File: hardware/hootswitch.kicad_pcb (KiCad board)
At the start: 2 copper layers, 100 x 88 mm, 127 parts, among them J1 Mini-DIN-4-G, J10 POWSEL, J11 TWI, J12 TWI, J2 Mini-DIN-4-G, J3 Mini-DIN-4-G, J4 Mini-DIN-4-G, J5 Mini-DIN-4-G, J6 Mini-DIN-4-G, J7 Barrel_Jack_MountingPin, J8 EXT_POW, J9 SW1, Q1 MMBT3904, Q10 MMBT3904, Q11 MMBT3904, Q12 MMBT3904, Q13 MMBT3904, Q14 MMBT3904, Q15 MMBT3904, Q16 MMBT3904, Q2 MMBT3904, Q3 MMBT3904, Q4 MMBT3904, Q5 MMBT3904, Q6 MMBT3904, Q7 MMBT3904, Q8 MMBT3904, Q9 MMBT3904, SW1 Switch1, U1 PicoW, U10 LTV-357T, U11 LTV-357T, U2 LM1117-5.0, U3 ADuM1201AR, U4 ADuM1201AR, U5 ADuM1201AR, U6 ADuM1201AR, U7 ADuM1201AR, U8 LTV-357T, U9 LTV-357T

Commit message: Increase resistance for the green LEDs
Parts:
- R14, R15, R16, R17: value 1K -> 1K8
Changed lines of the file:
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@@
       (effects (font (size 1 1) (thickness 0.15)))
     )
-    (fp_text value "1K" (at 0 1.43 90) (layer "F.Fab")
+    (fp_text value "1K8" (at 0 1.43 90) (layer "F.Fab")
       (effects (font (size 1 1) (thickness 0.15)))
     )
@@
       (effects (font (size 1 1) (thickness 0.15)))
     )
-    (fp_text value "1K" (at 0 1.43 90) (layer "F.Fab")
+    (fp_text value "1K8" (at 0 1.43 90) (layer "F.Fab")
       (effects (font (size 1 1) (thickness 0.15)))
     )
@@
       (effects (font (size 1 1) (thickness 0.15)))
     )
-    (fp_text value "1K" (at 0 1.43 90) (layer "F.Fab")
+    (fp_text value "1K8" (at 0 1.43 90) (layer "F.Fab")
       (effects (font (size 1 1) (thickness 0.15)))
     )
@@
       (effects (font (size 1 1) (thickness 0.15)))
     )
-    (fp_text value "1K" (at 0 1.43 90) (layer "F.Fab")
+    (fp_text value "1K8" (at 0 1.43 90) (layer "F.Fab")
       (effects (font (size 1 1) (thickness 0.15)))
     )

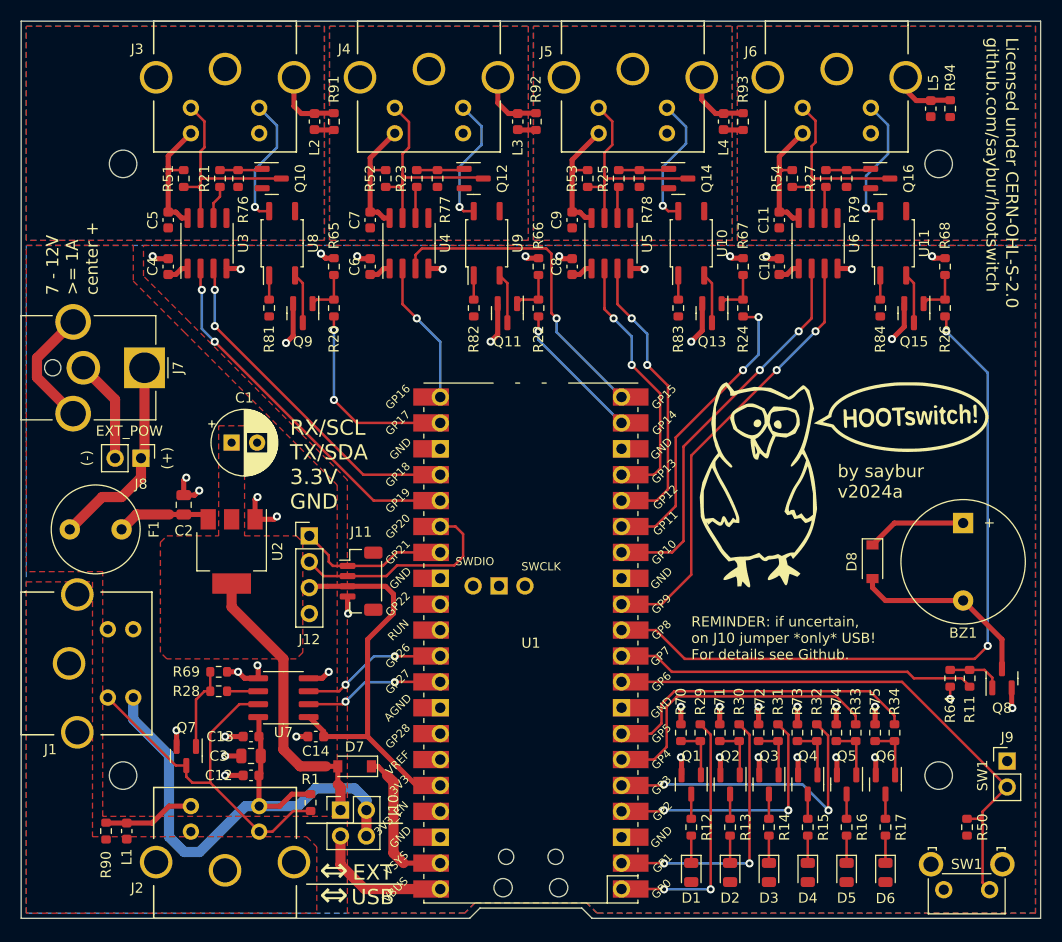
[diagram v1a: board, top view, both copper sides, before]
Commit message: Increase mounting hole size to support M3 screws.
These will require small head screws, they are very close to other items. This may require further board modifications.
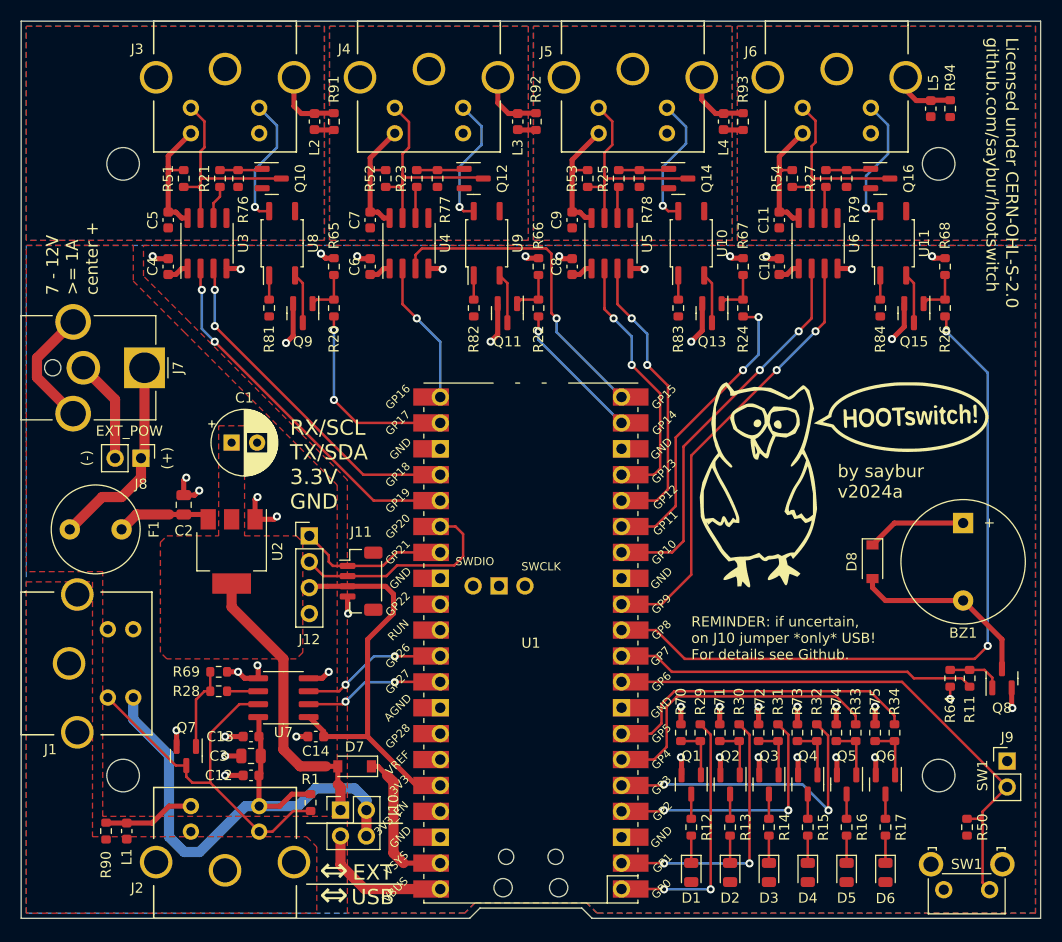
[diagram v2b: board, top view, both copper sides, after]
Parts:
- H1, H2, H3, H4: footprint MountingHole:MountingHole_2.7mm_M2.5 -> MountingHole:MountingHole_3.2mm_M3
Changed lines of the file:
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@@
     )
   )
-  (footprint "MountingHole:MountingHole_2.7mm_M2.5" (layer "F.Cu")
+  (footprint "MountingHole:MountingHole_3.2mm_M3" (layer "F.Cu")
     (at 70 74)
-    (descr "Mounting Hole 2.7mm, no annular, M2.5")
-    (tags "mounting hole 2.7mm no annular m2.5")
+    (descr "Mounting Hole 3.2mm, no annular, M3")
+    (tags "mounting hole 3.2mm no annular m3")
     (property "Sheetfile" "hootswitch.kicad_sch")
     (property "Sheetname" "")
     (clearance 2)
     (attr exclude_from_pos_files)
-    (fp_text reference "H2" (at 0 -3.7) (layer "F.SilkS") hide
+    (fp_text reference "H2" (at 0 -4.2) (layer "F.SilkS") hide
       (effects (font (size 1 1) (thickness 0.15)))
     )
-    (fp_text value "M" (at 0 3.7) (layer "F.Fab")
+    (fp_text value "M" (at 0 4.2) (layer "F.Fab") hide
       (effects (font (size 1 1) (thickness 0.15)))
     )
@@
       (effects (font (size 1 1) (thickness 0.15)))
     )
-    (fp_circle (center 0 0) (end 2.7 0) (layer "Cmts.User") (width 0.15) (fill none))
-    (fp_circle (center 0 0) (end 2.95 0) (layer "F.CrtYd") (width 0.05) (fill none))
-    (pad "" np_thru_hole circle (at 0 0) (size 2.7 2.7) (drill 2.7) (layers *.Cu *.Mask))
+    (fp_circle (center 0 0) (end 3.2 0) (layer "Cmts.User") (width 0.15) (fill none))
+    (fp_circle (center 0 0) (end 3.45 0) (layer "F.CrtYd") (width 0.05) (fill none))
+    (pad "" np_thru_hole circle (at 0 0) (size 3.2 3.2) (drill 3.2) (layers *.Cu *.Mask))
   )
   (footprint "Package_TO_SOT_SMD:SOT-23" (layer "F.Cu")
@@
     )
   )
-  (footprint "MountingHole:MountingHole_2.7mm_M2.5" (layer "F.Cu")
+  (footprint "MountingHole:MountingHole_3.2mm_M3" (layer "F.Cu")
     (at 150 74)
-    (descr "Mounting Hole 2.7mm, no annular, M2.5")
-    (tags "mounting hole 2.7mm no annular m2.5")
+    (descr "Mounting Hole 3.2mm, no annular, M3")
+    (tags "mounting hole 3.2mm no annular m3")
     (property "Sheetfile" "hootswitch.kicad_sch")
     (property "Sheetname" "")
     (clearance 2)
     (attr exclude_from_pos_files)
-    (fp_text reference "H4" (at 0 -3.7) (layer "F.SilkS") hide
+    (fp_text reference "H4" (at 0 -4.2) (layer "F.SilkS") hide
       (effects (font (size 1 1) (thickness 0.15)))
     )
-    (fp_text value "M" (at 0 3.7) (layer "F.Fab")
+    (fp_text value "M" (at 0 4.2) (layer "F.Fab")
       (effects (font (size 1 1) (thickness 0.15)))
     )
@@
       (effects (font (size 1 1) (thickness 0.15)))
     )
-    (fp_circle (center 0 0) (end 2.7 0) (layer "Cmts.User") (width 0.15) (fill none))
-    (fp_circle (center 0 0) (end 2.95 0) (layer "F.CrtYd") (width 0.05) (fill none))
-    (pad "" np_thru_hole circle (at 0 0) (size 2.7 2.7) (drill 2.7) (layers *.Cu *.Mask))
+    (fp_circle (center 0 0) (end 3.2 0) (layer "Cmts.User") (width 0.15) (fill none))
+    (fp_circle (center 0 0) (end 3.45 0) (layer "F.CrtYd") (width 0.05) (fill none))
+    (pad "" np_thru_hole circle (at 0 0) (size 3.2 3.2) (drill 3.2) (layers *.Cu *.Mask))
   )
   (footprint "Resistor_SMD:R_0603_1608Metric" (layer "F.Cu")
@@
     )
   )
-  (footprint "MountingHole:MountingHole_2.7mm_M2.5" (layer "F.Cu")
+  (footprint "MountingHole:MountingHole_3.2mm_M3" (layer "F.Cu")
     (at 150 134)
-    (descr "Mounting Hole 2.7mm, no annular, M2.5")
-    (tags "mounting hole 2.7mm no annular m2.5")
+    (descr "Mounting Hole 3.2mm, no annular, M3")
+    (tags "mounting hole 3.2mm no annular m3")
     (property "Sheetfile" "hootswitch.kicad_sch")
     (property "Sheetname" "")
     (clearance 2)
     (attr exclude_from_pos_files)
-    (fp_text reference "H3" (at 0 -3.7) (layer "F.SilkS") hide
+    (fp_text reference "H3" (at 0 -4.2) (layer "F.SilkS") hide
       (effects (font (size 1 1) (thickness 0.15)))
     )
-    (fp_text value "M" (at 0 3.7) (layer "F.Fab")
+    (fp_text value "M" (at 0 4.2) (layer "F.Fab") hide
       (effects (font (size 1 1) (thickness 0.15)))
     )
@@
       (effects (font (size 1 1) (thickness 0.15)))
     )
-    (fp_circle (center 0 0) (end 2.7 0) (layer "Cmts.User") (width 0.15) (fill none))
-    (fp_circle (center 0 0) (end 2.95 0) (layer "F.CrtYd") (width 0.05) (fill none))
-    (pad "" np_thru_hole circle (at 0 0) (size 2.7 2.7) (drill 2.7) (layers *.Cu *.Mask))
+    (fp_circle (center 0 0) (end 3.2 0) (layer "Cmts.User") (width 0.15) (fill none))
+    (fp_circle (center 0 0) (end 3.45 0) (layer "F.CrtYd") (width 0.05) (fill none))
+    (pad "" np_thru_hole circle (at 0 0) (size 3.2 3.2) (drill 3.2) (layers *.Cu *.Mask))
   )
   (footprint "Package_SO:SO-4_4.4x3.9mm_P2.54mm" (layer "F.Cu")
@@
       (net 86 "Net-(J1-Pad5)") (pintype "passive"))
   )
-  (footprint "MountingHole:MountingHole_2.7mm_M2.5" (layer "F.Cu")
+  (footprint "MountingHole:MountingHole_3.2mm_M3" (layer "F.Cu")
     (at 70 134)
-    (descr "Mounting Hole 2.7mm, no annular, M2.5")
-    (tags "mounting hole 2.7mm no annular m2.5")
+    (descr "Mounting Hole 3.2mm, no annular, M3")
+    (tags "mounting hole 3.2mm no annular m3")
     (property "Sheetfile" "hootswitch.kicad_sch")
     (property "Sheetname" "")
     (clearance 2)
     (attr exclude_from_pos_files)
-    (fp_text reference "H1" (at 0 -3.7) (layer "F.SilkS") hide
+    (fp_text reference "H1" (at 0 -4.2) (layer "F.SilkS") hide
       (effects (font (size 1 1) (thickness 0.15)))
     )
-    (fp_text value "M" (at 0 3.7) (layer "F.Fab")
+    (fp_text value "M" (at 0 4.2) (layer "F.Fab") hide
       (effects (font (size 1 1) (thickness 0.15)))
     )
@@
       (effects (font (size 1 1) (thickness 0.15)))
     )
-    (fp_circle (center 0 0) (end 2.7 0) (layer "Cmts.User") (width 0.15) (fill none))
-    (fp_circle (center 0 0) (end 2.95 0) (layer "F.CrtYd") (width 0.05) (fill none))
-    (pad "" np_thru_hole circle (at 0 0) (size 2.7 2.7) (drill 2.7) (layers *.Cu *.Mask))
+    (fp_circle (center 0 0) (end 3.2 0) (layer "Cmts.User") (width 0.15) (fill none))
+    (fp_circle (center 0 0) (end 3.45 0) (layer "F.CrtYd") (width 0.05) (fill none))
+    (pad "" np_thru_hole circle (at 0 0) (size 3.2 3.2) (drill 3.2) (layers *.Cu *.Mask))
   )
   (footprint "Resistor_SMD:R_0603_1608Metric" (layer "F.Cu")

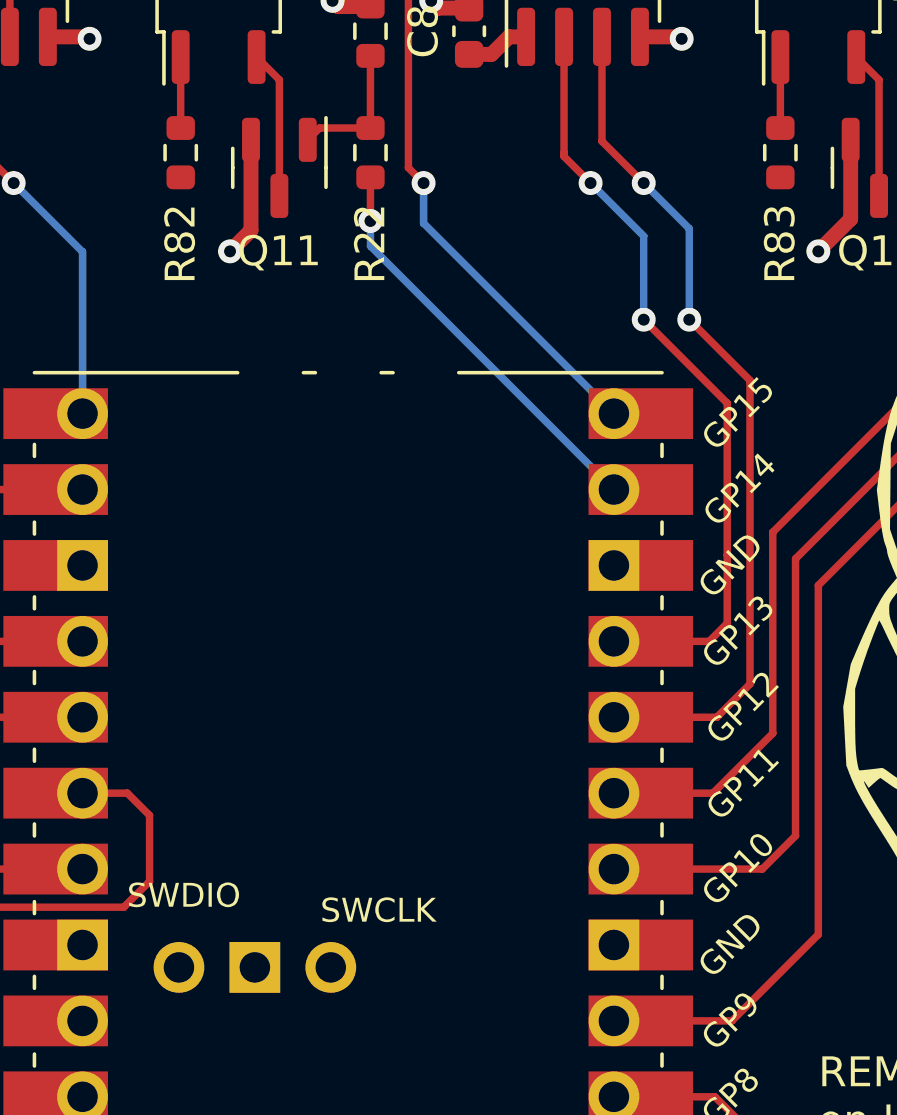
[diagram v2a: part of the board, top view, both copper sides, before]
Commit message: Added partial copper keepout for wireless module.
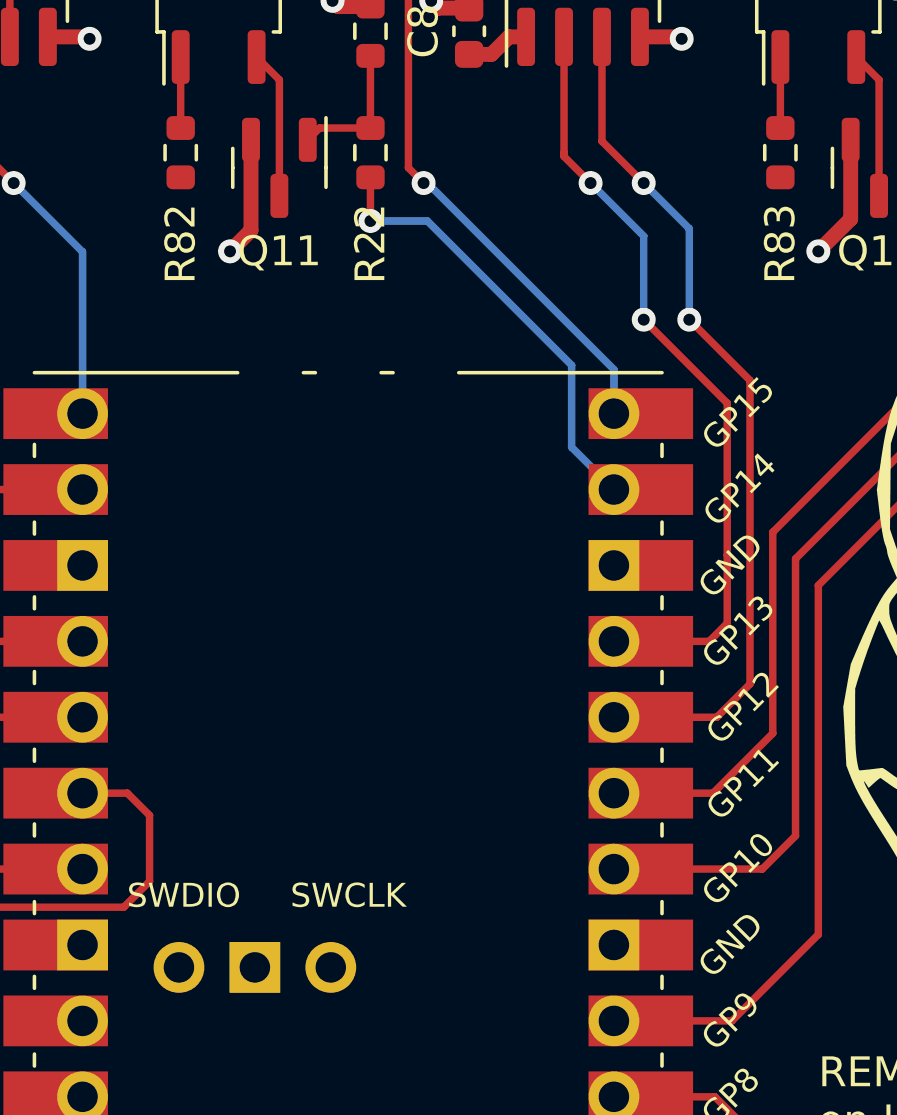
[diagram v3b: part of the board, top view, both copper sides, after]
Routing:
- net /C2_PSW: track 13.8 -> 14.9 mm
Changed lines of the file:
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@@
       (effects (font (size 0.8 0.8) (thickness 0.15)))
     )
-    (fp_text user "SWCLK" (at -1 7.5) (layer "F.SilkS")
+    (fp_text user "SWCLK" (at 0 8) (layer "F.SilkS")
       (effects (font (size 0.8 0.8) (thickness 0.15)))
     )
@@
   (segment (start 112.014 82.804) (end 111.506 82.296) (width 0.25) (layer "F.Cu") (net 74))
   (via (at 112.522 89.154) (size 0.8) (drill 0.4) (layers "F.Cu" "B.Cu") (net 74))
-  (segment (start 118.89 96.87) (end 112.522 90.502) (width 0.25) (layer "B.Cu") (net 74))
-  (segment (start 112.522 90.502) (end 112.522 89.154) (width 0.25) (layer "B.Cu") (net 74))
+  (segment (start 112.522 89.154) (end 112.649 89.154) (width 0.25) (layer "B.Cu") (net 74))
+  (segment (start 118.89 95.395) (end 118.89 96.87) (width 0.25) (layer "B.Cu") (net 74))
+  (segment (start 112.649 89.154) (end 118.89 95.395) (width 0.25) (layer "B.Cu") (net 74))
   (segment (start 110.744 90.424) (end 110.744 88.963) (width 0.25) (layer "F.Cu") (net 75))
   (via (at 110.744 90.424) (size 0.8) (drill 0.4) (layers "F.Cu" "B.Cu") (net 75))
-  (segment (start 110.744 91.264) (end 118.89 99.41) (width 0.25) (layer "B.Cu") (net 75))
-  (segment (start 110.744 90.424) (end 110.744 91.264) (width 0.25) (layer "B.Cu") (net 75))
+  (segment (start 117.475 95.25) (end 112.649 90.424) (width 0.25) (layer "B.Cu") (net 75))
+  (segment (start 118.89 99.41) (end 117.475 97.995) (width 0.25) (layer "B.Cu") (net 75))
+  (segment (start 117.475 97.995) (end 117.475 95.25) (width 0.25) (layer "B.Cu") (net 75))
+  (segment (start 112.649 90.424) (end 110.744 90.424) (width 0.25) (layer "B.Cu") (net 75))
   (segment (start 97.409 84.263) (end 97.409 87.757) (width 0.25) (layer "F.Cu") (net 76))
   (segment (start 97.409 87.757) (end 98.806 89.154) (width 0.25) (layer "F.Cu") (net 76))
@@
   (segment (start 89.67 114.435) (end 88.265 113.03) (width 0.25) (layer "F.Cu") (net 100))
   (segment (start 96.8756 113.3856) (end 102.489 113.3856) (width 0.25) (layer "F.Cu") (net 100))
+  (zone (net 0) (net_name "") (layers F&B.Cu "Edge.Cuts") (hatch edge 0.508)
+    (connect_pads (clearance 0))
+    (min_thickness 0.254)
+    (keepout (tracks allowed) (vias allowed) (pads allowed) (copperpour not_allowed) (footprints allowed))
+    (fill (thermal_gap 0.508) (thermal_bridge_width 0.508))
+    (polygon
+      (pts
+        (xy 116 104)
+        (xy 104 104)
+        (xy 104 94.615)
+        (xy 116 94.615)
+      )
+    )
+  )
   (zone (net 9) (net_name "Net-(C5-Pad2)") (layer "F.Cu") (hatch edge 0.508)
     (connect_pads (clearance 0.5))
